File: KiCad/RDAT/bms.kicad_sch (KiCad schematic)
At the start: 29 parts, among them Q1 NMOS, Q6 NMOS, U3 BQ7791500PWT, U4 BQ34Z100PWR-R2

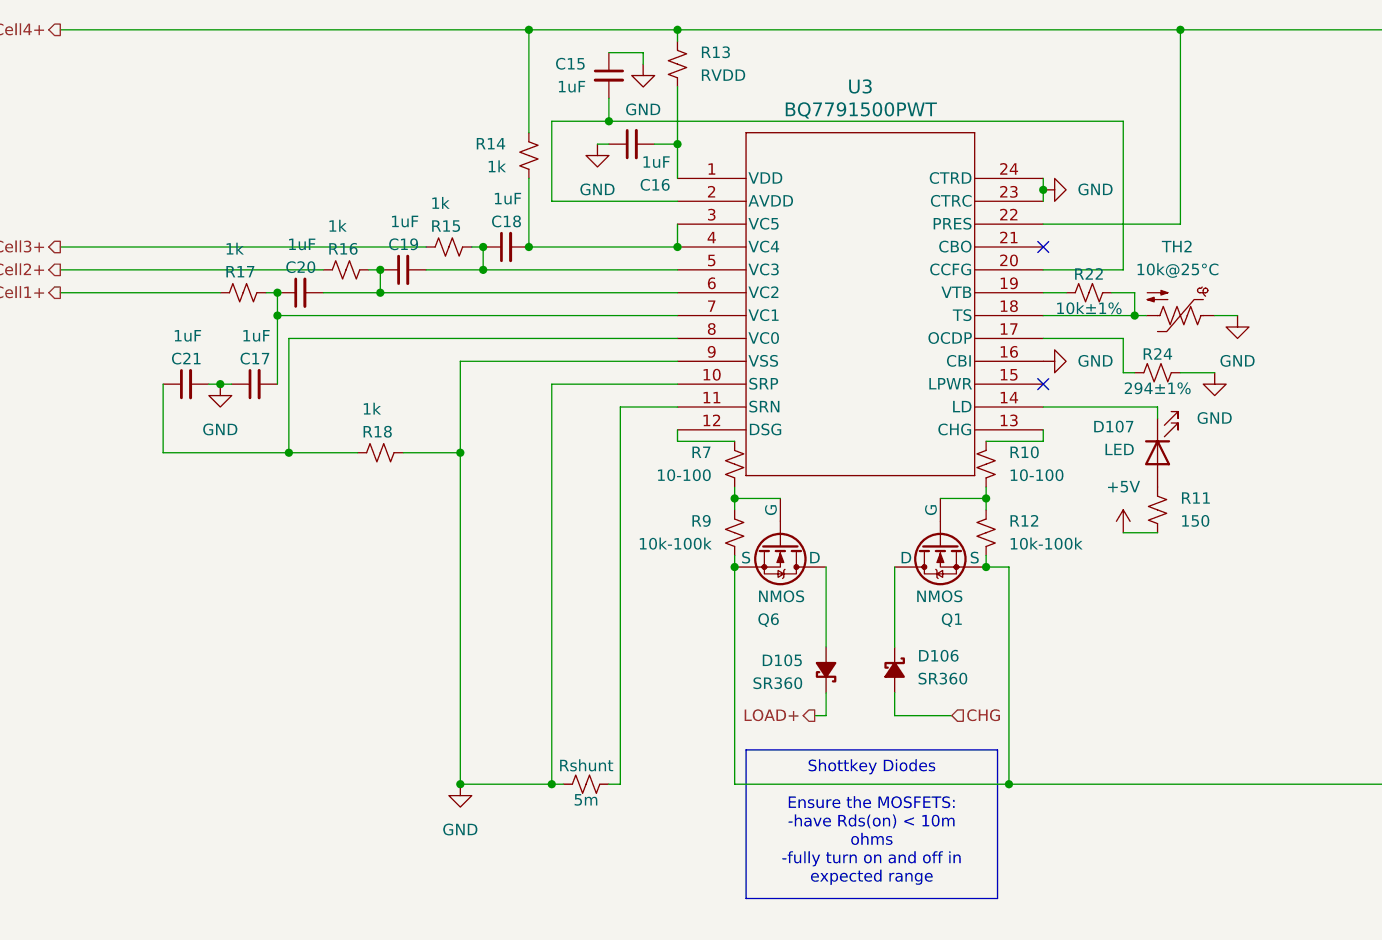
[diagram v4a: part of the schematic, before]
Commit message: Add new notes; update component references in schematics and footprints, and complete charging design
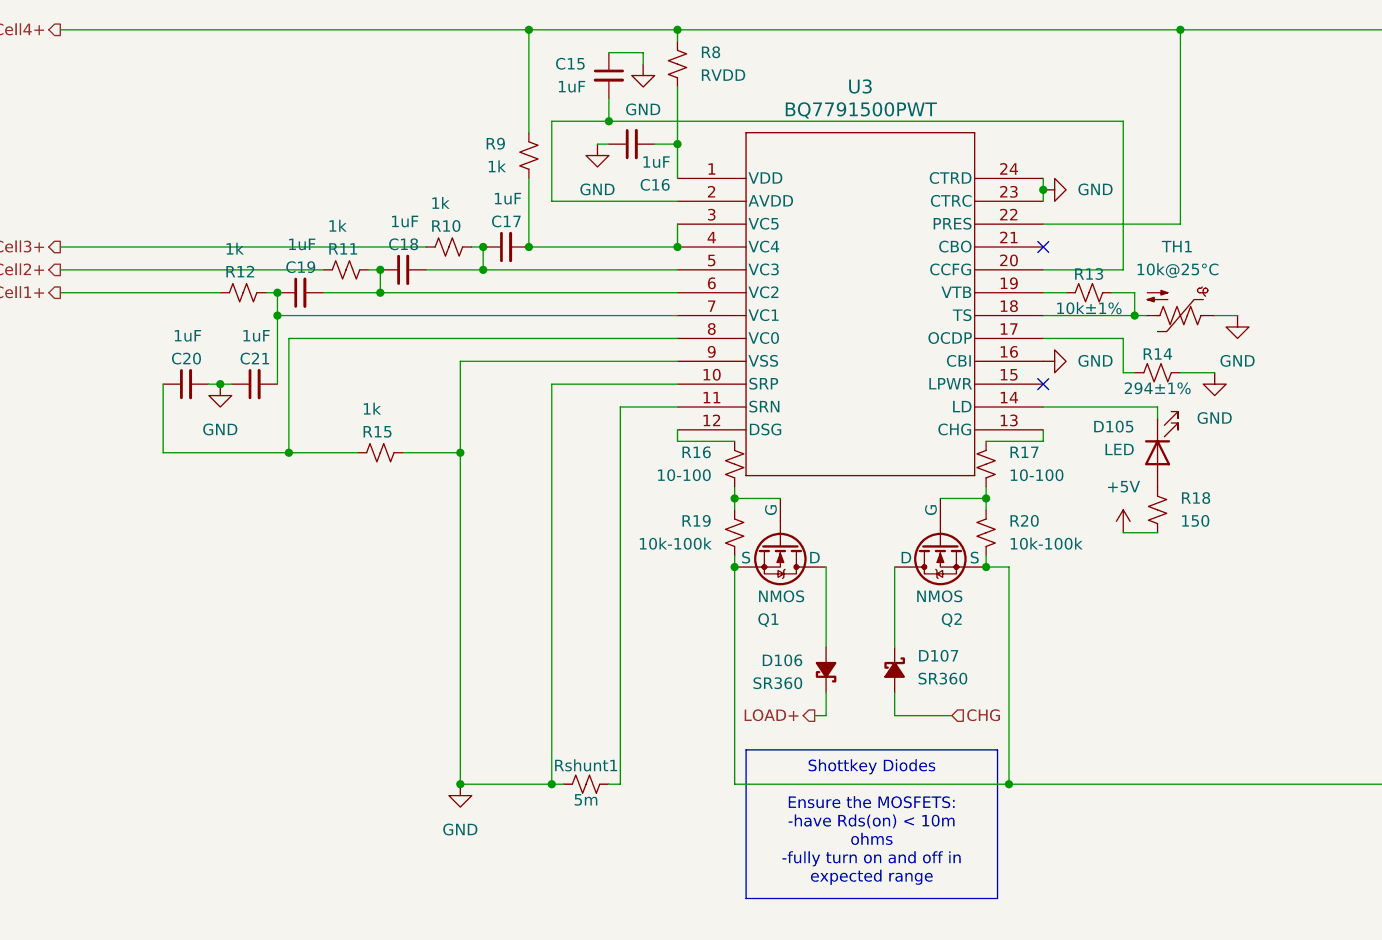
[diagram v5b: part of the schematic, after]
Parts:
- renumbered C18 to C17, C19 to C18, C20 to C19, C21 to C20, C17 to C21, D107 to D105, D105 to D106, D106 to D107, Q6 to Q1, Q1 to Q2, R15 to R10, R16 to R11, R17 to R12, R22 to R13, R24 to R14, R18 to R15, R7 to R16, R10 to R17, R11 to R18, R9 to R19, R12 to R20, R13 to R8, R14 to R9, Rshunt to Rshunt1, TH2 to TH1
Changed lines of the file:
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@@
 		(on_board yes)
 		(dnp no)
-		(property "Reference" "Q1"
+		(property "Reference" "Q2"
 			(at 120.65 79.502 90)
 			(effects
@@
 			(project "RDAT"
 				(path "/0db9370a-8a21-4fd2-83a9-f207c3725dc9/8352a856-8d2f-4632-b66f-b2f3049cf780"
-					(reference "Q1")
+					(reference "Q2")
 					(unit 1)
 				)
@@
 		(on_board yes)
 		(dnp no)
-		(property "Reference" "R22"
+		(property "Reference" "R13"
 			(at 134.62 41.148 90)
 			(effects
@@
 			(project "RDAT"
 				(path "/0db9370a-8a21-4fd2-83a9-f207c3725dc9/8352a856-8d2f-4632-b66f-b2f3049cf780"
-					(reference "R22")
+					(reference "R13")
 					(unit 1)
 				)
@@
 		(on_board yes)
 		(dnp no)
-		(property "Reference" "R18"
+		(property "Reference" "R15"
 			(at 53.848 58.674 90)
 			(effects
@@
 			(project "RDAT"
 				(path "/0db9370a-8a21-4fd2-83a9-f207c3725dc9/8352a856-8d2f-4632-b66f-b2f3049cf780"
-					(reference "R18")
+					(reference "R15")
 					(unit 1)
 				)
@@
 		(on_board yes)
 		(dnp no)
-		(property "Reference" "R16"
+		(property "Reference" "R11"
 			(at 50.038 38.354 90)
 			(effects
@@
 			(project "RDAT"
 				(path "/0db9370a-8a21-4fd2-83a9-f207c3725dc9/8352a856-8d2f-4632-b66f-b2f3049cf780"
-					(reference "R16")
+					(reference "R11")
 					(unit 1)
 				)
@@
 		(dnp no)
 		(fields_autoplaced yes)
-		(property "Reference" "#PWR029"
+		(property "Reference" "#PWR028"
 			(at 38.1 59.69 0)
 			(effects
@@
 			(project ""
 				(path "/0db9370a-8a21-4fd2-83a9-f207c3725dc9/8352a856-8d2f-4632-b66f-b2f3049cf780"
-					(reference "#PWR029")
+					(reference "#PWR028")
 					(unit 1)
 				)
@@
 		(dnp no)
 		(fields_autoplaced yes)
-		(property "Reference" "D106"
+		(property "Reference" "D107"
 			(at 115.57 83.5659 90)
 			(effects
@@
 			(project ""
 				(path "/0db9370a-8a21-4fd2-83a9-f207c3725dc9/8352a856-8d2f-4632-b66f-b2f3049cf780"
-					(reference "D106")
+					(reference "D107")
 					(unit 1)
 				)
@@
 		(dnp no)
 		(fields_autoplaced yes)
-		(property "Reference" "#PWR023"
+		(property "Reference" "#PWR024"
 			(at 135.89 31.75 0)
 			(effects
@@
 			(project ""
 				(path "/0db9370a-8a21-4fd2-83a9-f207c3725dc9/8352a856-8d2f-4632-b66f-b2f3049cf780"
-					(reference "#PWR023")
+					(reference "#PWR024")
 					(unit 1)
 				)
@@
 		(on_board yes)
 		(dnp no)
-		(property "Reference" "R9"
+		(property "Reference" "R19"
 			(at 92.71 68.5799 0)
 			(effects
@@
 			(project ""
 				(path "/0db9370a-8a21-4fd2-83a9-f207c3725dc9/8352a856-8d2f-4632-b66f-b2f3049cf780"
-					(reference "R9")
+					(reference "R19")
 					(unit 1)
 				)
@@
 		(on_board yes)
 		(dnp no)
-		(property "Reference" "C17"
+		(property "Reference" "C21"
 			(at 43.688 50.546 90)
 			(effects
@@
 			(project "RDAT"
 				(path "/0db9370a-8a21-4fd2-83a9-f207c3725dc9/8352a856-8d2f-4632-b66f-b2f3049cf780"
-					(reference "C17")
+					(reference "C21")
 					(unit 1)
 				)
@@
 		(on_board yes)
 		(dnp no)
-		(property "Reference" "R12"
+		(property "Reference" "R20"
 			(at 125.73 68.5799 0)
 			(effects
@@
 			(project "RDAT"
 				(path "/0db9370a-8a21-4fd2-83a9-f207c3725dc9/8352a856-8d2f-4632-b66f-b2f3049cf780"
-					(reference "R12")
+					(reference "R20")
 					(unit 1)
 				)
@@
 		(on_board yes)
 		(dnp no)
-		(property "Reference" "Rshunt"
+		(property "Reference" "Rshunt1"
 			(at 78.74 95.758 90)
 			(effects
@@
 			(project "RDAT"
 				(path "/0db9370a-8a21-4fd2-83a9-f207c3725dc9/8352a856-8d2f-4632-b66f-b2f3049cf780"
-					(reference "Rshunt")
+					(reference "Rshunt1")
 					(unit 1)
 				)
@@
 		(on_board yes)
 		(dnp no)
-		(property "Reference" "R7"
+		(property "Reference" "R16"
 			(at 92.71 60.9599 0)
 			(effects
@@
 			(project ""
 				(path "/0db9370a-8a21-4fd2-83a9-f207c3725dc9/8352a856-8d2f-4632-b66f-b2f3049cf780"
-					(reference "R7")
+					(reference "R16")
 					(unit 1)
 				)
@@
 		(dnp no)
 		(fields_autoplaced yes)
-		(property "Reference" "#PWR028"
+		(property "Reference" "#PWR023"
 			(at 80.01 33.02 0)
 			(effects
@@
 			(project "RDAT"
 				(path "/0db9370a-8a21-4fd2-83a9-f207c3725dc9/8352a856-8d2f-4632-b66f-b2f3049cf780"
-					(reference "#PWR028")
+					(reference "#PWR023")
 					(unit 1)
 				)
@@
 		(on_board yes)
 		(dnp no)
-		(property "Reference" "C19"
+		(property "Reference" "C18"
 			(at 60.198 37.846 90)
 			(effects
@@
 			(project "RDAT"
 				(path "/0db9370a-8a21-4fd2-83a9-f207c3725dc9/8352a856-8d2f-4632-b66f-b2f3049cf780"
-					(reference "C19")
+					(reference "C18")
 					(unit 1)
 				)
@@
 		(on_board yes)
 		(dnp no)
-		(property "Reference" "R15"
+		(property "Reference" "R10"
 			(at 61.468 35.814 90)
 			(effects
@@
 			(project "RDAT"
 				(path "/0db9370a-8a21-4fd2-83a9-f207c3725dc9/8352a856-8d2f-4632-b66f-b2f3049cf780"
-					(reference "R15")
+					(reference "R10")
 					(unit 1)
 				)
@@
 		(on_board yes)
 		(dnp no)
-		(property "Reference" "R13"
+		(property "Reference" "R8"
 			(at 91.44 16.5099 0)
 			(effects
@@
 			(project ""
 				(path "/0db9370a-8a21-4fd2-83a9-f207c3725dc9/8352a856-8d2f-4632-b66f-b2f3049cf780"
-					(reference "R13")
+					(reference "R8")
 					(unit 1)
 				)
@@
 		(dnp no)
 		(fields_autoplaced yes)
-		(property "Reference" "TH2"
+		(property "Reference" "TH1"
 			(at 144.4625 38.1 90)
 			(effects
@@
 			(project ""
 				(path "/0db9370a-8a21-4fd2-83a9-f207c3725dc9/8352a856-8d2f-4632-b66f-b2f3049cf780"
-					(reference "TH2")
+					(reference "TH1")
 					(unit 1)
 				)
@@
 		(on_board yes)
 		(dnp no)
-		(property "Reference" "R10"
+		(property "Reference" "R17"
 			(at 125.73 60.9599 0)
 			(effects
@@
 			(project "RDAT"
 				(path "/0db9370a-8a21-4fd2-83a9-f207c3725dc9/8352a856-8d2f-4632-b66f-b2f3049cf780"
-					(reference "R10")
+					(reference "R17")
 					(unit 1)
 				)
@@
 		(dnp no)
 		(fields_autoplaced yes)
-		(property "Reference" "#PWR025"
+		(property "Reference" "#PWR029"
 			(at 138.43 73.66 0)
 			(effects
@@
 			(project ""
 				(path "/0db9370a-8a21-4fd2-83a9-f207c3725dc9/8352a856-8d2f-4632-b66f-b2f3049cf780"
-					(reference "#PWR025")
+					(reference "#PWR029")
 					(unit 1)
 				)
@@
 		(on_board yes)
 		(dnp no)
-		(property "Reference" "R17"
+		(property "Reference" "R12"
 			(at 38.608 40.894 90)
 			(effects
@@
 			(project "RDAT"
 				(path "/0db9370a-8a21-4fd2-83a9-f207c3725dc9/8352a856-8d2f-4632-b66f-b2f3049cf780"
-					(reference "R17")
+					(reference "R12")
 					(unit 1)
 				)
@@
 		(on_board yes)
 		(dnp no)
-		(property "Reference" "Q6"
+		(property "Reference" "Q1"
 			(at 97.79 79.502 90)
 			(effects
@@
 			(project "RDAT"
 				(path "/0db9370a-8a21-4fd2-83a9-f207c3725dc9/8352a856-8d2f-4632-b66f-b2f3049cf780"
-					(reference "Q6")
+					(reference "Q1")
 					(unit 1)
 				)
@@
 		(on_board yes)
 		(dnp no)
-		(property "Reference" "C20"
+		(property "Reference" "C19"
 			(at 48.768 40.386 90)
 			(effects
@@
 			(project "RDAT"
 				(path "/0db9370a-8a21-4fd2-83a9-f207c3725dc9/8352a856-8d2f-4632-b66f-b2f3049cf780"
-					(reference "C20")
+					(reference "C19")
 					(unit 1)
 				)
@@
 		(on_board yes)
 		(dnp no)
-		(property "Reference" "C18"
+		(property "Reference" "C17"
 			(at 71.628 35.306 90)
 			(effects
@@
 			(project "RDAT"
 				(path "/0db9370a-8a21-4fd2-83a9-f207c3725dc9/8352a856-8d2f-4632-b66f-b2f3049cf780"
-					(reference "C18")
+					(reference "C17")
 					(unit 1)
 				)
@@
 		(on_board yes)
 		(dnp no)
-		(property "Reference" "C21"
+		(property "Reference" "C20"
 			(at 36.068 50.546 90)
 			(effects
@@
 			(project "RDAT"
 				(path "/0db9370a-8a21-4fd2-83a9-f207c3725dc9/8352a856-8d2f-4632-b66f-b2f3049cf780"
-					(reference "C21")
+					(reference "C20")
 					(unit 1)
 				)
@@
 		(dnp no)
 		(fields_autoplaced yes)
-		(property "Reference" "#PWR024"
+		(property "Reference" "#PWR027"
 			(at 148.59 58.42 0)
 			(effects
@@
 			(project "RDAT"
 				(path "/0db9370a-8a21-4fd2-83a9-f207c3725dc9/8352a856-8d2f-4632-b66f-b2f3049cf780"
-					(reference "#PWR024")
+					(reference "#PWR027")
 					(unit 1)
 				)
@@
 		(dnp no)
 		(fields_autoplaced yes)
-		(property "Reference" "R11"
+		(property "Reference" "R18"
 			(at 144.78 66.0399 0)
 			(effects
@@
 			(project "RDAT"
 				(path "/0db9370a-8a21-4fd2-83a9-f207c3725dc9/8352a856-8d2f-4632-b66f-b2f3049cf780"
-					(reference "R11")
+					(reference "R18")
 					(unit 1)
 				)
@@
 		(on_board yes)
 		(dnp no)
-		(property "Reference" "D105"
+		(property "Reference" "D106"
 			(at 102.87 84.0739 90)
 			(effects
@@
 			(project ""
 				(path "/0db9370a-8a21-4fd2-83a9-f207c3725dc9/8352a856-8d2f-4632-b66f-b2f3049cf780"
-					(reference "D105")
+					(reference "D106")
 					(unit 1)
 				)
@@
 		(on_board yes)
 		(dnp no)
-		(property "Reference" "R24"
+		(property "Reference" "R14"
 			(at 142.24 50.038 90)
 			(effects
@@
 			(project "RDAT"
 				(path "/0db9370a-8a21-4fd2-83a9-f207c3725dc9/8352a856-8d2f-4632-b66f-b2f3049cf780"
-					(reference "R24")
+					(reference "R14")
 					(unit 1)
 				)
@@
 		(on_board yes)
 		(dnp no)
-		(property "Reference" "D107"
+		(property "Reference" "D105"
 			(at 139.7 58.1024 90)
 			(effects
@@
 			(project ""
 				(path "/0db9370a-8a21-4fd2-83a9-f207c3725dc9/8352a856-8d2f-4632-b66f-b2f3049cf780"
-					(reference "D107")
+					(reference "D105")
 					(unit 1)
 				)
@@
 		(on_board yes)
 		(dnp no)
-		(property "Reference" "R14"
+		(property "Reference" "R9"
 			(at 69.85 26.6699 0)
 			(effects
@@
 			(project ""
 				(path "/0db9370a-8a21-4fd2-83a9-f207c3725dc9/8352a856-8d2f-4632-b66f-b2f3049cf780"
-					(reference "R14")
+					(reference "R9")
 					(unit 1)
 				)
@@
 		(dnp no)
 		(fields_autoplaced yes)
-		(property "Reference" "#PWR027"
+		(property "Reference" "#PWR025"
 			(at 151.13 52.07 0)
 			(effects
@@
 			(project "RDAT"
 				(path "/0db9370a-8a21-4fd2-83a9-f207c3725dc9/8352a856-8d2f-4632-b66f-b2f3049cf780"
-					(reference "#PWR027")
-					(unit 1)
-				)
+					(reference "#PWR025")
+					(unit 1)
+				)

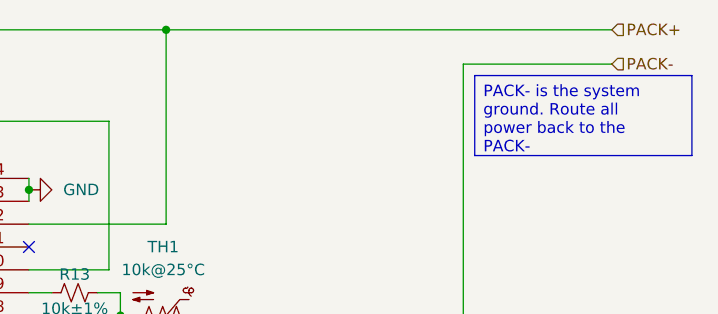
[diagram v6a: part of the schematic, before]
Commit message: Modified Power Stages
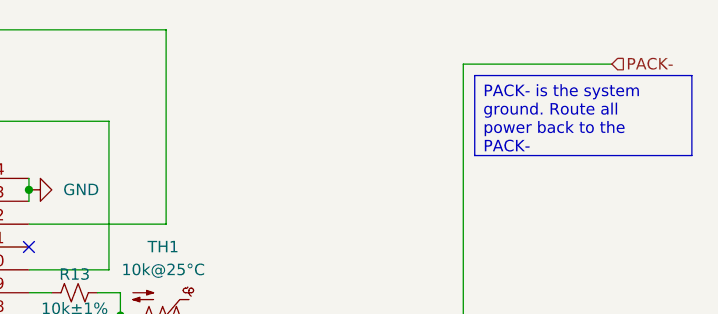
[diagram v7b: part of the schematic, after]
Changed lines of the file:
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@@
-	)
-	(junction
-		(at 144.78 13.97)
-		(diameter 0)
-		(color 0 0 0 0)
 	)
 	(junction
@@
 	(wire
 		(pts
-			(xy 144.78 13.97) (xy 194.31 13.97)
-		)
-		(stroke
-			(width 0)
-			(type default)
-		)
-	)
-	(wire
-		(pts
 			(xy 38.1 43.18) (xy 20.32 43.18)
 		)
@@
 		)
 	)
-	(hierarchical_label "PACK+"
-		(shape input)
-		(at 194.31 13.97 0)
-		(effects
-			(font
-				(size 1.27 1.27)
-			)
-			(justify left)
-		)
-	)

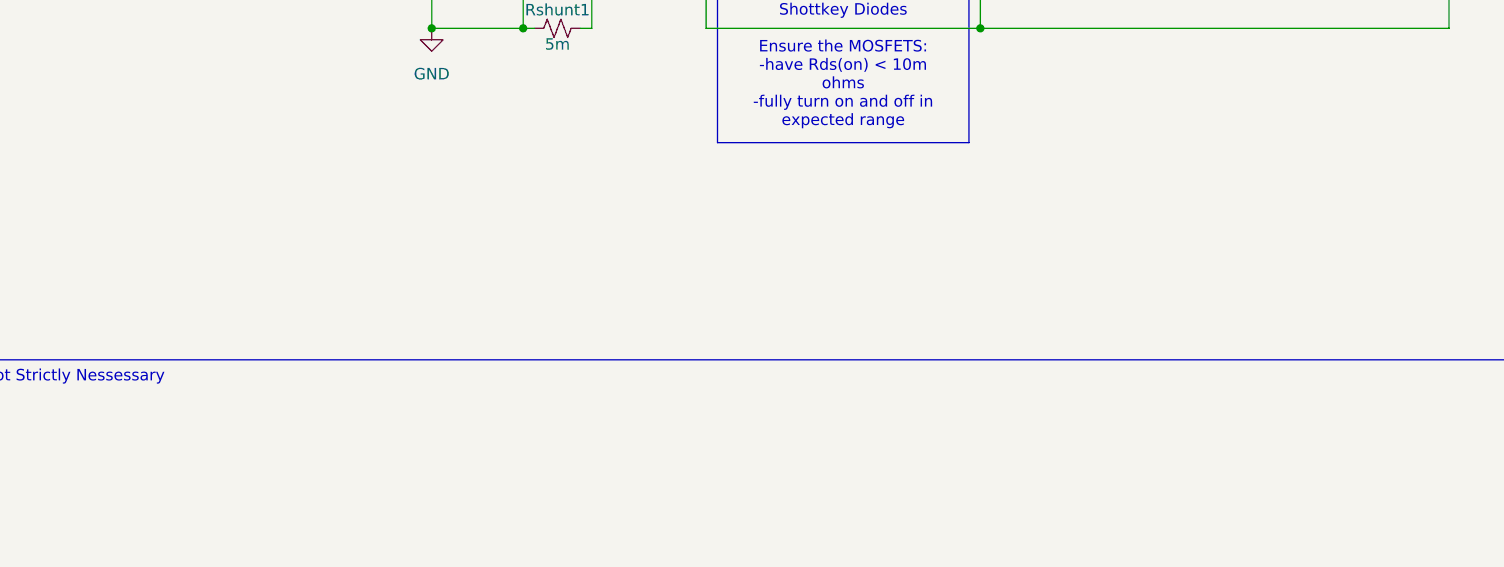
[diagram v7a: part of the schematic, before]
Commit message: Added HDMI connection and marked section for review in schematics; updated column widths in PRL file; added new operating values CSV files for power calculations.
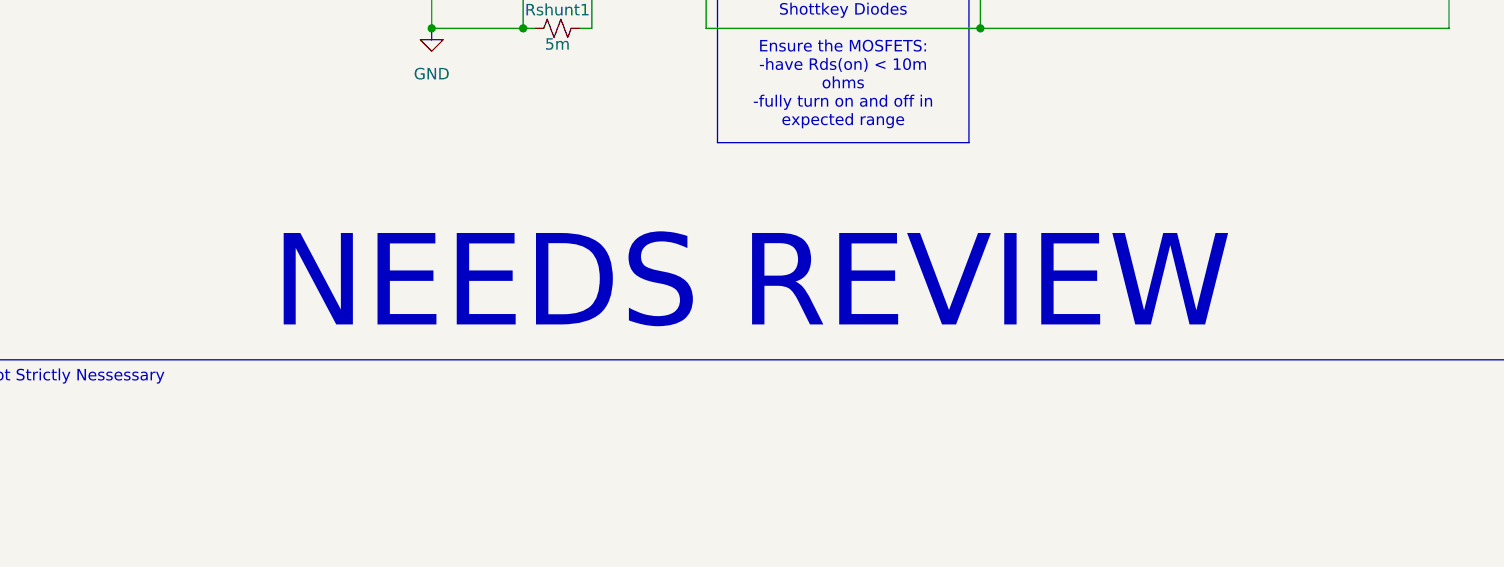
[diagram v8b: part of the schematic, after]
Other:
- note added: "NEEDS REVIEW"
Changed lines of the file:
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@@
 		(rev "0")
+	)
+	(text "NEEDS REVIEW"
+		(exclude_from_sim no)
+		(at 100.33 126.238 0)
+		(effects
+			(font
+				(size 10.16 10.16)
+			)
+		)
 	)
 	(text_box "Not Strictly Nessessary"
